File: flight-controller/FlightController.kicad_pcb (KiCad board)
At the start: 2 copper layers, 40 x 37 mm, 30 parts, among them J1 MSD-4-A, J2 Conn_01x03_Pin, J3 Conn_01x03_Pin, J4 Conn_01x03_Pin, J5 Conn_01x03_Pin, J6 USB4215-03-A_REVA, J7 Conn_01x03_Pin, J8 Conn_01x03_Pin, U1 ESP32-S3-WROOM-1, U2 TPS629210DRLR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

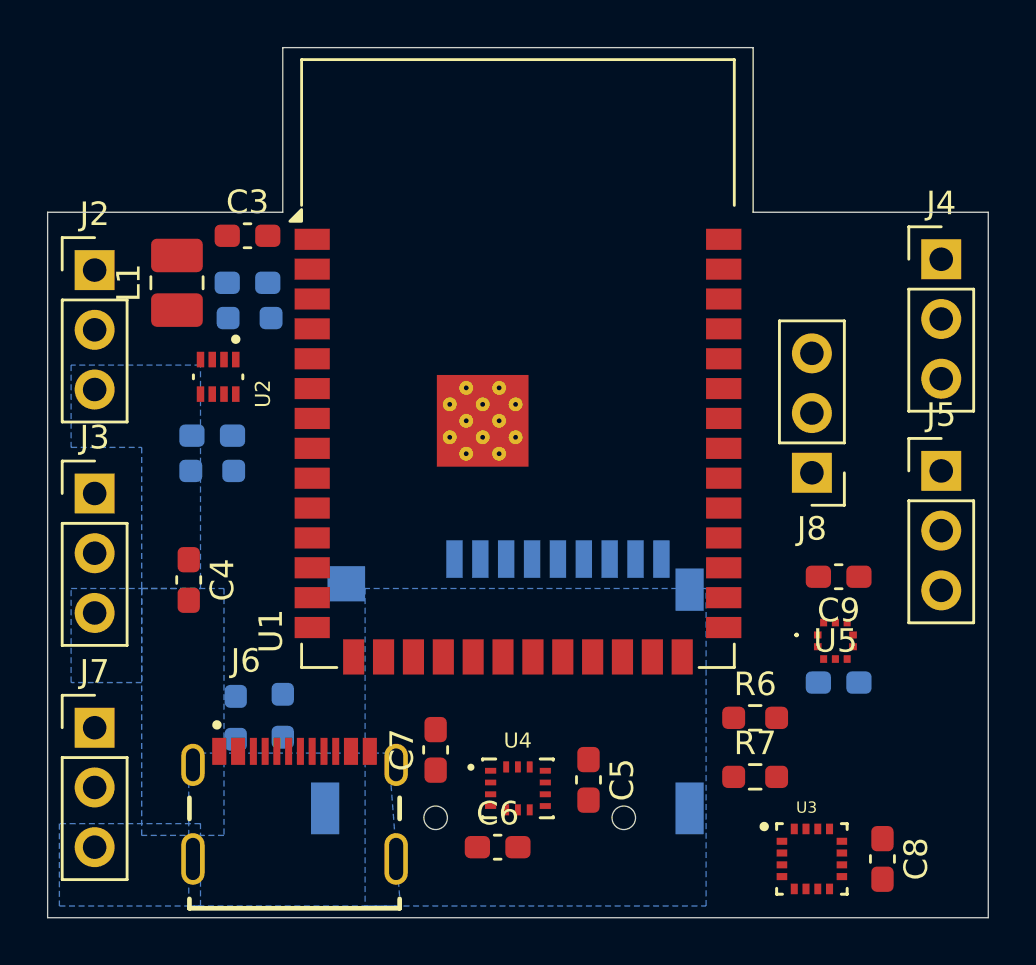
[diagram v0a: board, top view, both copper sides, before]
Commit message: DRC no errors
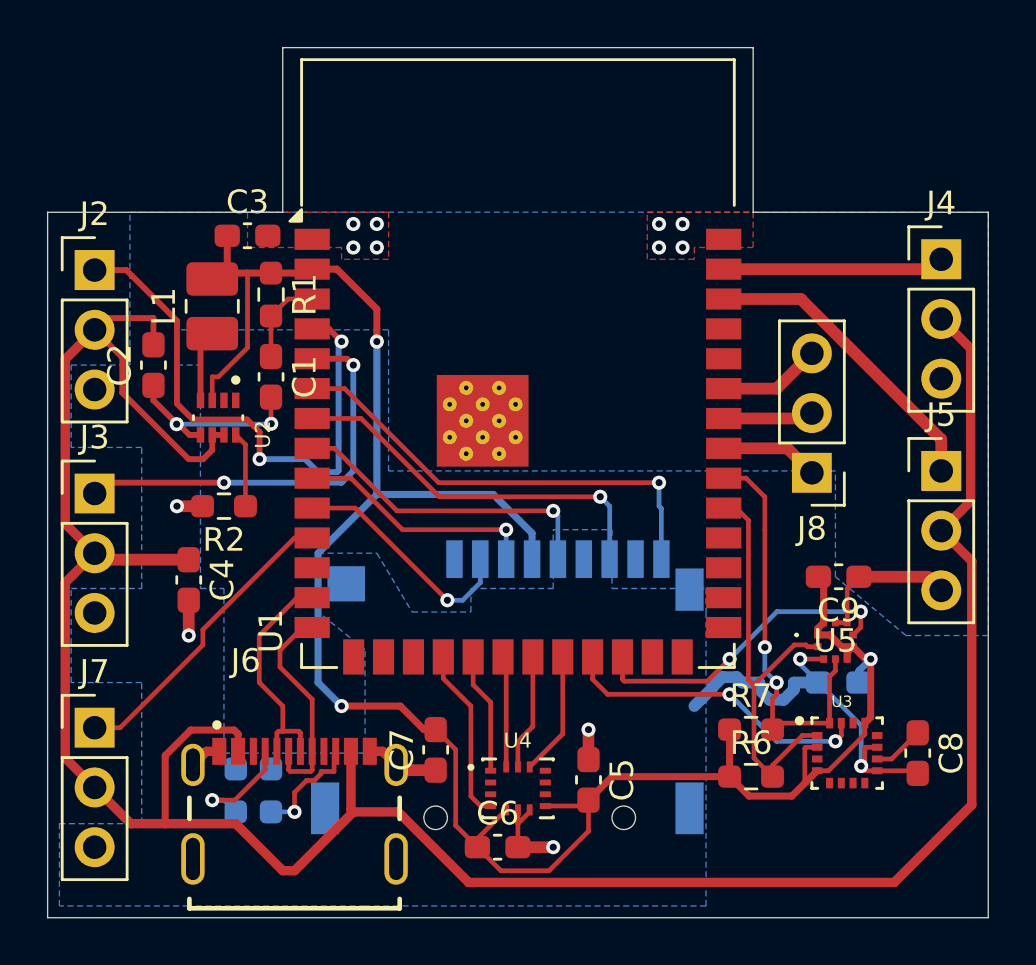
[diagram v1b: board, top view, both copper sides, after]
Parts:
- C1, C2, R1, R2: moved to F.Cu
- moved C8 4.74 mm to (127.0, 73.0)
- moved U3 4.74 mm to (124.0, 73.0)
- moved C1 4.12 mm to (99.5, 57.0), turned to -90 degrees
- moved C2 3.91 mm to (94.5, 56.5), turned to 90 degrees
- moved R3 3.21 mm to (99.5, 74.6), turned to -90 degrees
- moved R4 3.09 mm to (98.0, 74.6), turned to -90 degrees
- moved R6 2.51 mm to (119.9, 74.0)
- moved R7 2.02 mm to (119.9, 72.0)
- moved L1 1.80 mm to (97.0, 54.0)
- moved U2 1.73 mm to (97.2, 58.7)
- moved R2 1.58 mm to (97.5, 62.5)
- moved R1 1.35 mm to (99.5, 53.5), turned to -90 degrees
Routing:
- net +5V: track 0.00 -> 113.5 mm
- net +3.3V: track 0.00 -> 91.0 mm, vias 0 -> 3
- net GND: track 0.00 -> 44.8 mm, vias 0 -> 16
- net MOTOR1_PWM: track 0.00 -> 23.7 mm, vias 0 -> 2
- net SD_CD: track 0.00 -> 19.7 mm, vias 0 -> 1
- net I2C_SCL: track 0.00 -> 18.9 mm
- net MOTOR2_PWM: track 0.00 -> 17.8 mm, vias 0 -> 2
- net I2C_SDA: track 0.00 -> 17.6 mm, vias 0 -> 2
- net SD_MISO: track 0.00 -> 16.5 mm, vias 0 -> 1
- net SD_CLK: track 0.00 -> 13.5 mm, vias 0 -> 1
- net BARO_INT: track 0.00 -> 13.5 mm, vias 0 -> 2
- net MAG_INT: track 0.00 -> 13.2 mm, vias 0 -> 2
- net MOTOR4_PWM: track 0.00 -> 13.1 mm
- net RECEIVER: track 0.00 -> 13.0 mm
- net SD_MOSI: track 0.00 -> 10.4 mm, vias 0 -> 1
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- added copper zone on F.Cu, net GND
